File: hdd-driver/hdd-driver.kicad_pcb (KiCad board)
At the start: 2 copper layers, 74 x 76 mm, 20 parts, among them J1 12V IN, J2 HDD motor contacts, U1 WeAct STM32G474CEU6 Core Board, U2 SimpleFOC Mini v1.0 (DRV8313), U3 MT3608 module, set to 12 V

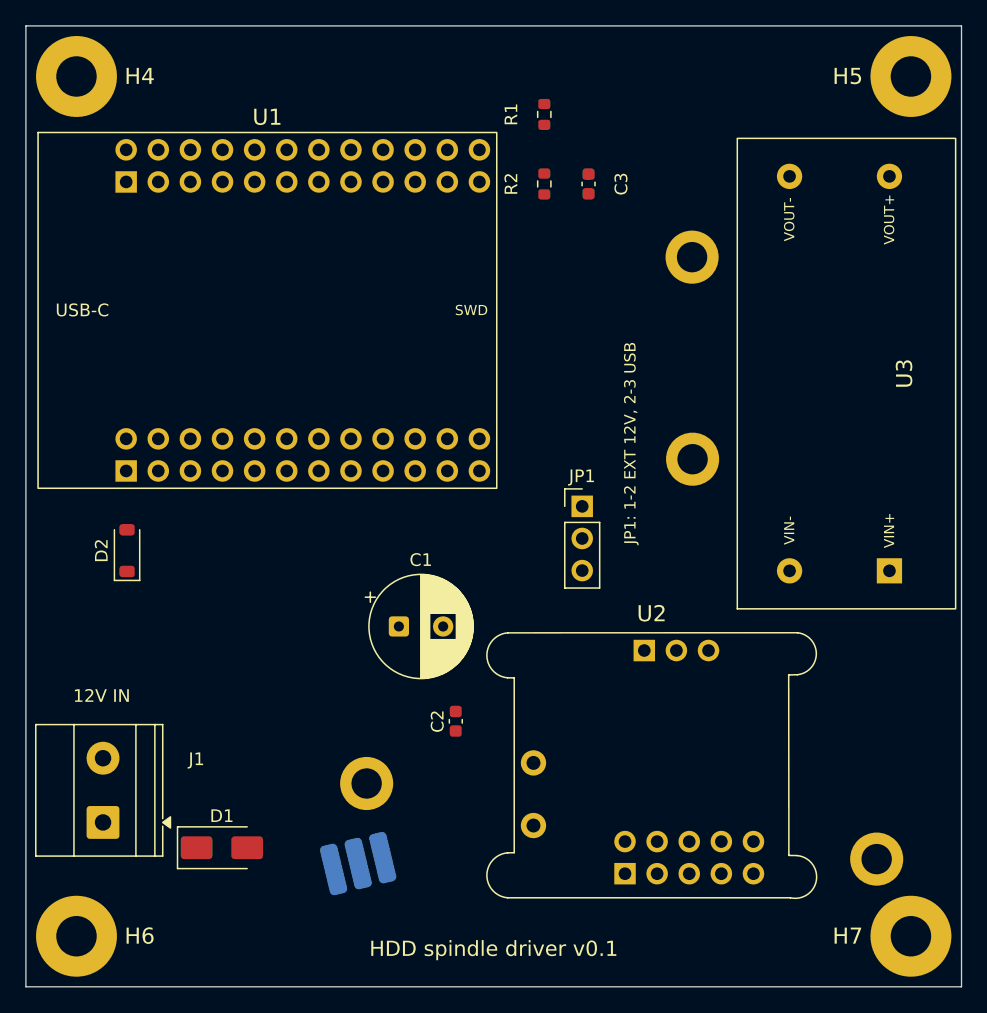
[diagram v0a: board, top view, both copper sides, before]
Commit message: hdd-driver: cut 3 mm off the top edge, add 1 mm component edge keepout
The board's top edge overhung the drive's connector end by 3 mm; it is now
flush with it (outline Y 0..73, 74 x 73 mm). Corner holes H4/H5 moved down
with it and now overlap the U1/U3 courtyards (open).

A rule area "EdgeKeepout" plus a custom rule in hdd-driver.kicad_dru keep
component courtyards 1 mm from the edge; footprints excluded from the BOM
(mounting holes) are exempt.

Also includes in-progress placement changes made in KiCad (U1 rotated,
J1/D1/D2 moved off-board) and KiCad's project file updates.
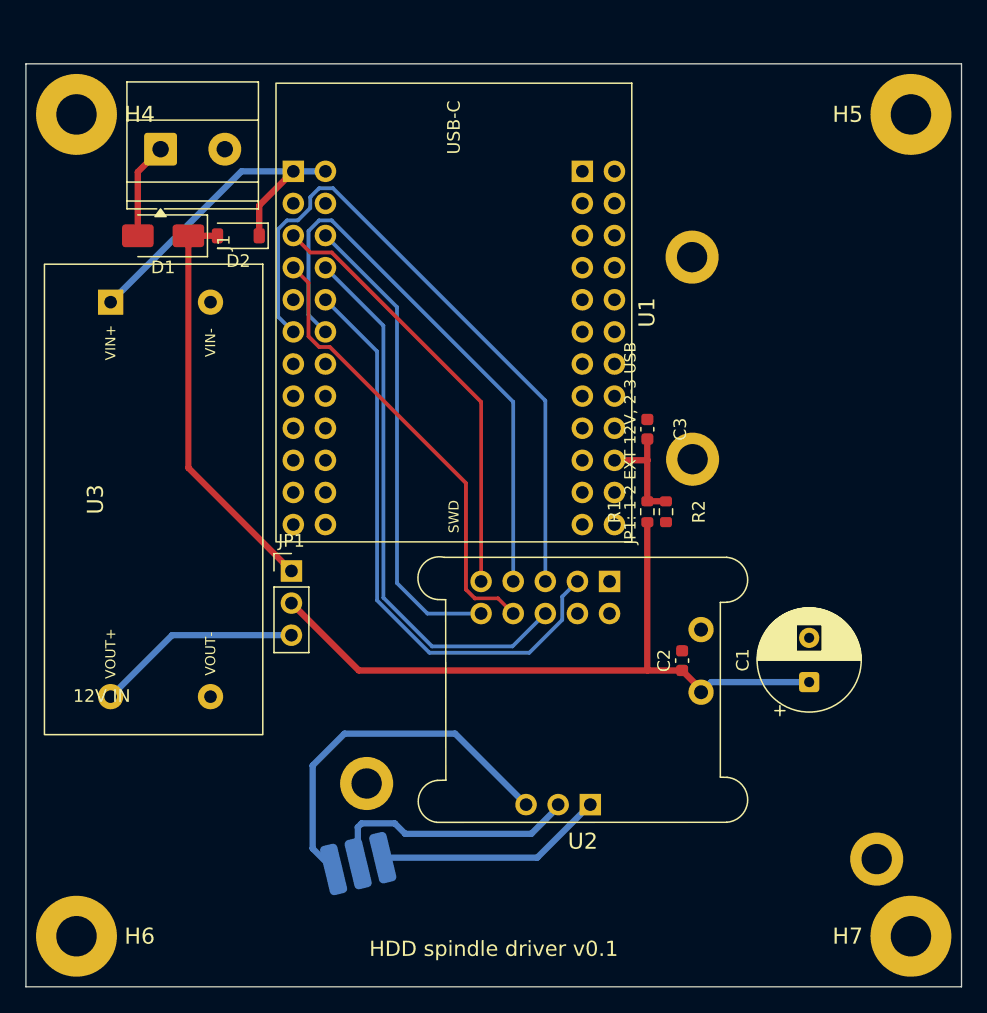
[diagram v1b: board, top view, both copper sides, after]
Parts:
- moved U3 55.7 mm to (124.1, 74.5), turned to -90 degrees
- moved J1 53.4 mm to (124.7, 46.8), turned to 0 degrees
- moved D1 48.6 mm to (124.8, 53.6), turned to 180 degrees
- moved C1 32.7 mm to (175.9, 88.9), turned to 90 degrees
- moved R1 32.5 mm to (163.2, 75.4)
- moved R2 27.7 mm to (164.6, 75.4), turned to -90 degrees
- moved D2 26.4 mm to (130.8, 53.6), turned to 180 degrees
- moved JP1 23.6 mm to (135.0, 80.1)
- moved C3 19.9 mm to (163.2, 68.9)
- moved C2 18.5 mm to (165.9, 87.2)
- moved U1 14.8 mm to (147.8, 59.7), turned to -90 degrees
- moved U2 8.11 mm to (158.0, 89.5), turned to 0 degrees
- moved H4 3.00 mm to (118.0, 44.0)
- moved H5 3.00 mm to (184.0, 44.0)
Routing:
- net /VM: track 0.00 -> 56.1 mm
- net /DRV_IN2: track 0.00 -> 52.8 mm
- net /DRV_IN1: track 0.00 -> 46.4 mm
- net /DRV_IN3: track 0.00 -> 45.2 mm
- net /DRV_nRESET: track 0.00 -> 43.5 mm
- net /DRV_nFAULT: track 0.00 -> 37.5 mm
- net /DRV_nSLEEP: track 0.00 -> 36.1 mm
- net /DRV_EN: track 0.00 -> 34.5 mm
- net /+12V: track 0.00 -> 32.2 mm
- net /PH_A: track 0.00 -> 29.2 mm
- net /VCC_MCU: track 0.00 -> 27.5 mm
- net /PH_B: track 0.00 -> 20.3 mm
- net /PH_C: track 0.00 -> 18.2 mm
- net /VBOOST: track 0.00 -> 16.3 mm
- net /VM_SENSE: track 0.00 -> 9.00 mm
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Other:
- board size 74 x 76 mm -> 74 x 73 mm

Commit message: hdd-driver: add GND pours on both layers and stitching vias
GND_TOP (F.Cu) and GND_BOTTOM (B.Cu) cover the whole board with 0.3 mm
clearance and thermal reliefs. The rule area J2_SpringKeepout (J2's
B.CrtYd) keeps the bottom pour and vias away from the spring pads.

76 GND stitching vias (0.6/0.3 mm): about every 5 mm round the edge and
on a 10 mm grid inside, only where both pours have copper. DRC: 0
unconnected items.
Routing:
- net GND: vias 0 -> 76
- added copper zone on B.Cu, net GND
- added copper zone on F.Cu, net GND

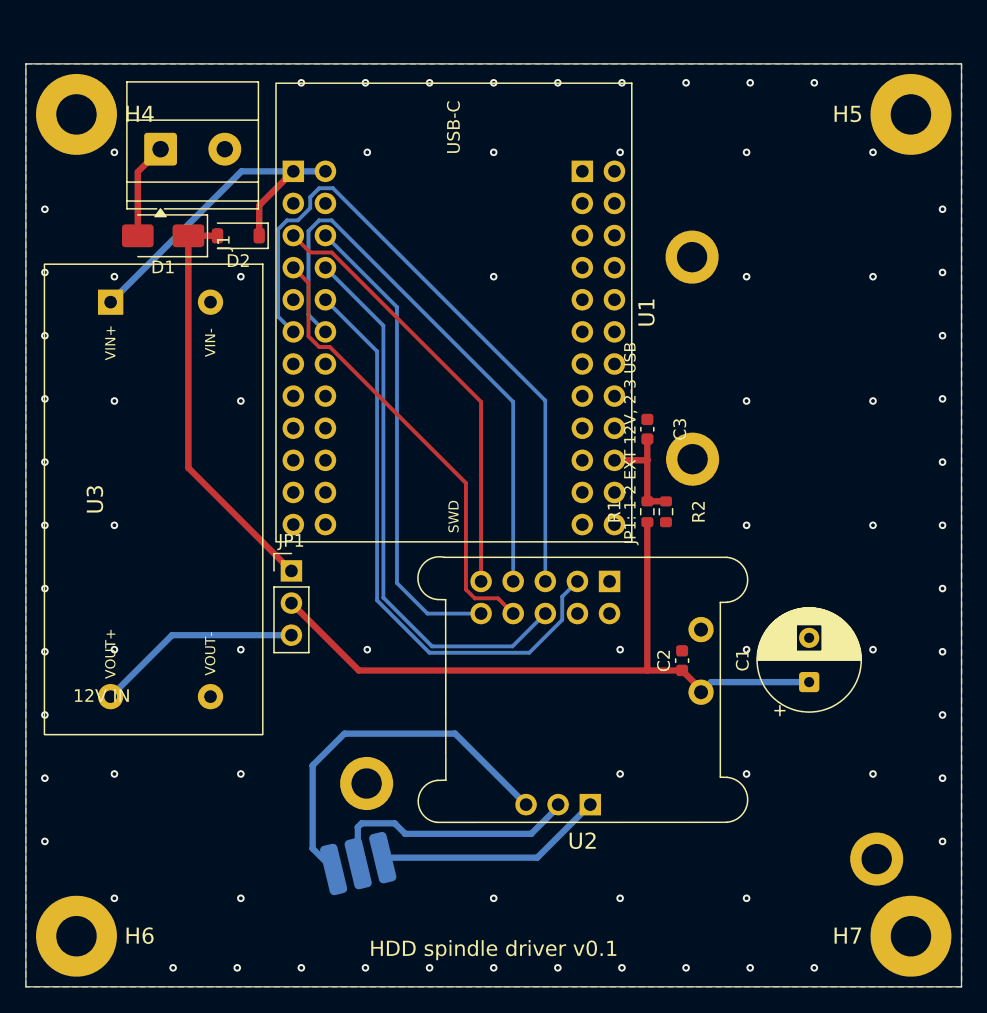
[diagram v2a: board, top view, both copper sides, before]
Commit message: hdd-driver: add current sensing and VR coil input, route the board
Schematic:
- RS1 20 mOhm bus shunt between VM and the new net VM_DRV (SimpleFOC "+",
  C1, C2), read by U4 INA181A2 into I_BUS (PA3).
- RS2/RS3 20 mOhm inline in phases A/B, read by U5/U6 INA240A1 (REF at
  mid-supply) into I_A (PA2) and I_B (PA4). U5's inputs are swapped for
  the layout, so I_A reads with the opposite sign.
- J3 VR coil terminal: 22k series resistor, BAV99 clamp and 470 pF filter
  into PA1 (COMP1_INP / ADC12_IN2), biased by a 10k/10k divider.

PCB: the shunt areas are routed by hand with Kelvin sense legs and the
tracks are locked; the phase tracks reach the spring pads on B.Cu from
below. The remaining signal nets were routed with KiCadRoutingTools and
cleaned up; track ends were re-joined after the final part nudges. DRC
with schematic parity: 0 violations, 0 unconnected. Zones are saved
filled.

README and CLAUDE.md: pin table, power diagram, routing notes.
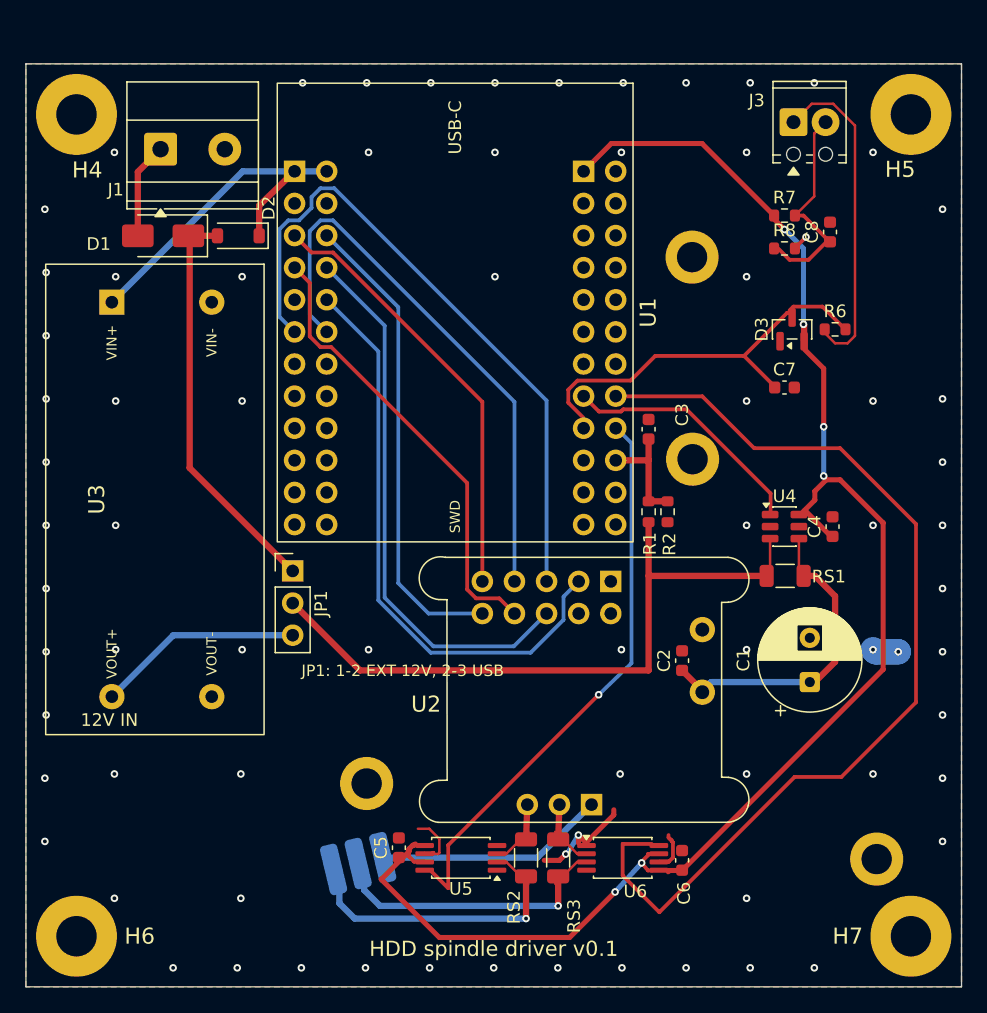
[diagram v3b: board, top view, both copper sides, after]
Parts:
- added C4: 100nF, Capacitor_SMD:C_0603_1608Metric, F.Cu at (177.8, 76.6)
- added C5: 100nF, Capacitor_SMD:C_0603_1608Metric, F.Cu at (143.5, 102.0)
- added C6: 100nF, Capacitor_SMD:C_0603_1608Metric, F.Cu at (165.9, 103.0)
- added C7: 470pF, Capacitor_SMD:C_0603_1608Metric, F.Cu at (174.0, 65.6)
- added C8: 1uF, Capacitor_SMD:C_0603_1608Metric, F.Cu at (177.6, 53.3)
- added D3: BAV99, Package_TO_SOT_SMD:SOT-23, F.Cu at (174.6, 61.0)
- added J3: VR coil, TerminalBlock_Phoenix:TerminalBlock_Phoenix_MPT-0,5-2-2.54_1x02_P2.54mm_Horizontal, F.Cu at (174.7, 44.6)
- added R6: 22k, Resistor_SMD:R_0603_1608Metric, F.Cu at (178.0, 61.0)
- added R7: 10k, Resistor_SMD:R_0603_1608Metric, F.Cu at (174.0, 52.0)
- added R8: 10k, Resistor_SMD:R_0603_1608Metric, F.Cu at (174.0, 54.6)
- added RS1: 20m, Resistor_SMD:R_1206_3216Metric, F.Cu at (174.1, 80.5)
- added RS2: 20m, Resistor_SMD:R_1206_3216Metric, F.Cu at (153.6, 102.8)
- added RS3: 20m, Resistor_SMD:R_1206_3216Metric, F.Cu at (156.1, 102.8)
- added U4: INA181A2, Package_TO_SOT_SMD:SOT-23-6, F.Cu at (174.0, 76.6)
- added U5: INA240A1PW, Package_SO:TSSOP-8_4.4x3mm_P0.65mm, F.Cu at (148.4, 102.8)
- added U6: INA240A1PW, Package_SO:TSSOP-8_4.4x3mm_P0.65mm, F.Cu at (161.2, 102.8)
- moved R2 0.12 mm to (164.8, 75.4)
- moved U3 0.10 mm to (124.2, 74.5)
- moved C3 0.10 mm to (163.2, 68.9)
- moved JP1 0.10 mm to (135.1, 80.1)
- moved R1 0.10 mm to (163.2, 75.4)
- moved U1 0.10 mm to (147.9, 59.7)
- moved U2 0.10 mm to (158.1, 89.5)
- moved C1 0.05 mm to (176.0, 88.9)
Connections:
- C1 pad 1: /VM -> /VM_DRV
- C2 pad 1: /VM -> /VM_DRV
- U1 pad P2.1: unconnected-(U1-3V3-PadP2.1) -> /3V3
- U1 pad P2.15: unconnected-(U1-PA3-PadP2.15) -> /I_BUS
- U1 pad P2.16: unconnected-(U1-PA4-PadP2.16) -> /I_B
- U1 pad P2.17: unconnected-(U1-PA1-PadP2.17) -> /VR_IN
- U1 pad P2.18: unconnected-(U1-PA2-PadP2.18) -> /I_A
- U2 pad 11: /VM -> /VM_DRV
- U2 pad 13: /PH_A -> /PH_A_DRV
- U2 pad 14: /PH_B -> /PH_B_DRV
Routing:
- net /3V3: track 0.00 -> 121.2 mm, vias 0 -> 6
- net /I_B: track 0.00 -> 78.1 mm
- net /I_A: track 0.00 -> 44.9 mm, vias 0 -> 1
- net /VR_IN: track 0.00 -> 31.6 mm
- net /VR_P: track 0.00 -> 25.8 mm
- net /VM_DRV: track 0.00 -> 24.7 mm
- net GND: track 0.00 -> 22.2 mm, vias 76 -> 75
- net /I_BUS: track 0.00 -> 19.8 mm
- net /VR_BIAS: track 0.00 -> 16.8 mm
- net /PH_A: track 29.2 -> 22.9 mm, vias 0 -> 1
- net /PH_B_DRV: track 0.00 -> 5.94 mm
- net /PH_A_DRV: track 0.00 -> 5.94 mm
- net /VM: track 56.1 -> 53.9 mm
- net /PH_B: track 20.3 -> 21.7 mm, vias 0 -> 1
